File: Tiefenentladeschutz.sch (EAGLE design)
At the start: 22 parts, among them IC1 ICL7665CSA, Q4 NMOSFET-D2PAK-7, T1 BC856B

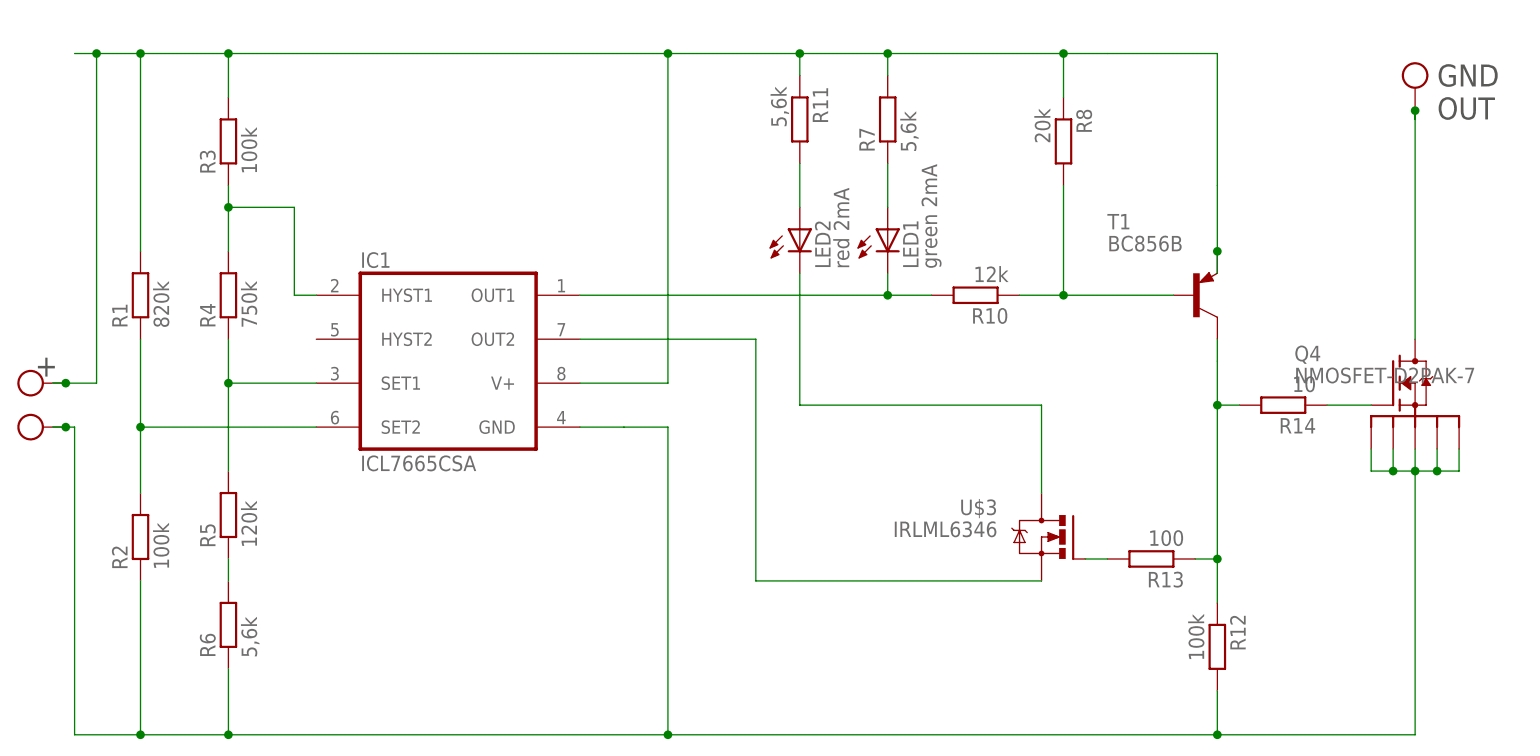
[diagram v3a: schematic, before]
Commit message: Smaller Resistors, less transistors, smaller pcb
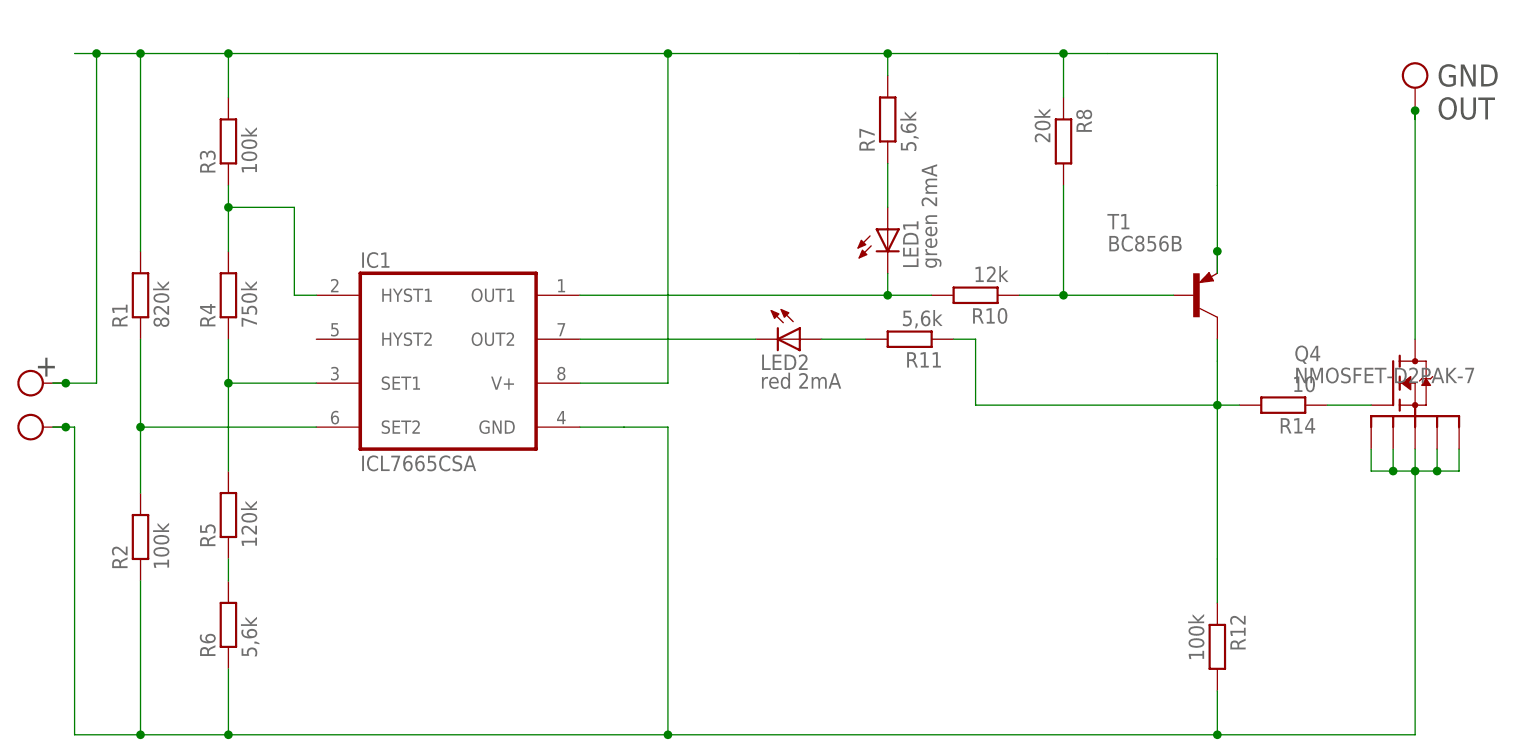
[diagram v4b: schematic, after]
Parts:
- removed R13: 100, rcl:R-EU_R1206
- removed U$3: IRLML6346, 0liver:IRLML6346
- R1, R10, R11, R2, R5, R6: device eagle-ltspice:RR1206 -> rcl:R-EU_R0603
- R3: device rcl:R-EU_R0603 -> rcl:R-EU_M1206
- U$4: device 0liver:PINBIG -> 0liver:PIN2.54
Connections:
- removed net N$11: LED2.C, U$3.D
- removed net N$9: R13.2, U$3.G
- net N$22: now also R11.1; no longer R13.1
- net N$3: now also LED2.C; no longer U$3.S
- net V+: no longer R11.1
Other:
- moved on the sheet: LED2, R11
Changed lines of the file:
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@@
 <?xml version="1.0" encoding="utf-8"?>
 <!DOCTYPE eagle SYSTEM "eagle.dtd">
-<eagle version="8.0.1">
+<eagle version="8.2.1">
 <drawing>
 <settings>
@@
 <layer number="48" name="Document" color="7" fill="1" visible="no" active="no"/>
 <layer number="49" name="Reference" color="7" fill="1" visible="no" active="no"/>
+<layer number="50" name="dxf" color="7" fill="1" visible="no" active="no"/>
 <layer number="51" name="tDocu" color="7" fill="1" visible="no" active="no"/>
 <layer number="52" name="bDocu" color="7" fill="1" visible="no" active="no"/>
+<layer number="53" name="tPadExt" color="7" fill="1" visible="no" active="no"/>
+<layer number="54" name="bPadExt" color="1" fill="1" visible="no" active="no"/>
 <layer number="90" name="Modules" color="5" fill="1" visible="yes" active="yes"/>
 <layer number="91" name="Nets" color="2" fill="1" visible="yes" active="yes"/>
@@
 <layer number="98" name="Guide" color="6" fill="1" visible="yes" active="yes"/>
 <layer number="99" name="SpiceOrder" color="5" fill="1" visible="yes" active="yes"/>
+<layer number="200" name="200bmp" color="1" fill="10" visible="no" active="no"/>
+<layer number="250" name="Descript" color="3" fill="1" visible="no" active="no"/>
+<layer number="251" name="SMDround" color="12" fill="11" visible="no" active="no"/>
 </layers>
 <schematic xreflabel="%F%N/%S.%C%R" xrefpart="/%S.%C%R">
@@
 <parts>
 <part name="R4" library="rcl" deviceset="R-EU_" device="R0603" value="750k"/>
-<part name="R5" library="eagle-ltspice" deviceset="R" device="R1206" value="120k"/>
-<part name="R1" library="eagle-ltspice" deviceset="R" device="R1206" value="820k"/>
-<part name="R2" library="eagle-ltspice" deviceset="R" device="R1206" value="100k"/>
-<part name="R11" library="eagle-ltspice" deviceset="R" device="R1206" value="5,6k"/>
+<part name="R5" library="rcl" deviceset="R-EU_" device="R0603" value="120k"/>
+<part name="R1" library="rcl" deviceset="R-EU_" device="R0603" value="820k"/>
+<part name="R2" library="rcl" deviceset="R-EU_" device="R0603" value="100k"/>
+<part name="R11" library="rcl" deviceset="R-EU_" device="R0603" value="5,6k"/>
 <part name="R8" library="rcl" deviceset="R-EU_" device="R0603" value="20k"/>
 <part name="IC1" library="maxim" deviceset="ICL7665CSA" device=""/>
@@
 <part name="LED1" library="eagle-ltspice" deviceset="LED_E" device="SML0603" value="green 2mA"/>
 <part name="R7" library="rcl" deviceset="R-EU_" device="R0603" value="5,6k"/>
-<part name="R10" library="eagle-ltspice" deviceset="R" device="R1206" value="12k"/>
-<part name="R6" library="eagle-ltspice" deviceset="R" device="R1206" value="5,6k"/>
-<part name="R3" library="rcl" deviceset="R-EU_" device="R0603" value="100k"/>
+<part name="R10" library="rcl" deviceset="R-EU_" device="R0603" value="12k"/>
+<part name="R6" library="rcl" deviceset="R-EU_" device="R0603" value="5,6k"/>
+<part name="R3" library="rcl" deviceset="R-EU_" device="M1206" value="100k"/>
 <part name="R12" library="eagle-ltspice" deviceset="R" device="R1206" value="100k"/>
-<part name="U$3" library="0liver" deviceset="IRLML6346" device=""/>
-<part name="U$4" library="0liver" deviceset="PIN" device="BIG"/>
+<part name="U$4" library="0liver" deviceset="PIN" device="2.54"/>
 <part name="U$6" library="0liver" deviceset="PIN" device="1.27"/>
 <part name="U$7" library="0liver" deviceset="PIN" device="1.27"/>
 <part name="Q4" library="D2pak-7" deviceset="NMOSFET-D2PAK-7" device=""/>
-<part name="R13" library="rcl" deviceset="R-EU_" device="R1206" value="100"/>
 <part name="R14" library="rcl" deviceset="R-EU_" device="R0603" value="10"/>
 <part name="T1" library="transistor" deviceset="*-PNP-" device="SOT23-BEC" technology="BC856B" value="BC856B"/>
@@
 <instance part="R1" gate="G$1" x="-20.32" y="68.58" rot="R90"/>
 <instance part="R2" gate="G$1" x="-20.32" y="40.64" rot="R90"/>
-<instance part="R11" gate="G$1" x="55.88" y="88.9" rot="R270"/>
+<instance part="R11" gate="G$1" x="68.58" y="63.5" rot="R180"/>
 <instance part="R8" gate="G$1" x="86.36" y="86.36" rot="R270"/>
 <instance part="IC1" gate="G$1" x="15.24" y="60.96"/>
-<instance part="LED2" gate="G$1" x="55.88" y="76.2"/>
+<instance part="LED2" gate="G$1" x="55.88" y="63.5" rot="R270"/>
 <instance part="LED1" gate="G$1" x="66.04" y="76.2"/>
 <instance part="R7" gate="G$1" x="66.04" y="88.9" rot="R90"/>
@@
 <instance part="R3" gate="G$1" x="-10.16" y="86.36" rot="R90"/>
 <instance part="R12" gate="G$1" x="104.14" y="27.94" rot="R270"/>
-<instance part="U$3" gate="G$1" x="86.36" y="40.64" rot="MR0"/>
 <instance part="U$4" gate="G$1" x="-33.02" y="58.42" rot="R90"/>
 <instance part="U$6" gate="G$1" x="-33.02" y="53.34" rot="R90"/>
 <instance part="U$7" gate="G$1" x="127" y="93.98"/>
 <instance part="Q4" gate="G$1" x="124.46" y="58.42"/>
-<instance part="R13" gate="G$1" x="96.52" y="38.1" rot="R180"/>
 <instance part="R14" gate="G$1" x="111.76" y="55.88" rot="R180"/>
 <instance part="T1" gate="G$1" x="101.6" y="68.58"/>
@@
 </segment>
 </net>
-<net name="N$5" class="0">
-<segment>
-<pinref part="R11" gate="G$1" pin="2"/>
-<pinref part="LED2" gate="G$1" pin="A"/>
-<wire x1="55.88" y1="83.82" x2="55.88" y2="78.74" width="0.1524" layer="91"/>
-</segment>
-</net>
 <net name="N$6" class="0">
 <segment>
@@
 <junction x="104.14" y="55.88"/>
 <wire x1="104.14" y1="38.1" x2="104.14" y2="55.88" width="0.1524" layer="91"/>
-<wire x1="104.14" y1="38.1" x2="101.6" y2="38.1" width="0.1524" layer="91"/>
-<junction x="104.14" y="38.1"/>
 <wire x1="104.14" y1="60.96" x2="104.14" y2="55.88" width="0.1524" layer="91"/>
 <wire x1="104.14" y1="55.88" x2="106.68" y2="55.88" width="0.1524" layer="91"/>
-<pinref part="R13" gate="G$1" pin="1"/>
 <pinref part="R14" gate="G$1" pin="2"/>
 <pinref part="T1" gate="G$1" pin="C"/>
 <wire x1="104.14" y1="63.5" x2="104.14" y2="60.96" width="0.1524" layer="91"/>
+<pinref part="R11" gate="G$1" pin="1"/>
+<wire x1="73.66" y1="63.5" x2="76.2" y2="63.5" width="0.1524" layer="91"/>
+<wire x1="76.2" y1="63.5" x2="76.2" y2="55.88" width="0.1524" layer="91"/>
+<wire x1="104.14" y1="55.88" x2="76.2" y2="55.88" width="0.1524" layer="91"/>
 </segment>
 </net>
@@
 <pinref part="R8" gate="G$1" pin="1"/>
 <wire x1="86.36" y1="96.52" x2="86.36" y2="91.44" width="0.1524" layer="91"/>
-<pinref part="R11" gate="G$1" pin="1"/>
-<wire x1="55.88" y1="96.52" x2="55.88" y2="93.98" width="0.1524" layer="91"/>
 <pinref part="R7" gate="G$1" pin="2"/>
 <wire x1="66.04" y1="96.52" x2="66.04" y2="93.98" width="0.1524" layer="91"/>
@@
 <wire x1="-20.32" y1="73.66" x2="-20.32" y2="96.52" width="0.1524" layer="91"/>
 <junction x="-20.32" y="96.52"/>
-<junction x="55.88" y="96.52"/>
 <junction x="66.04" y="96.52"/>
 <wire x1="-10.16" y1="96.52" x2="-10.16" y2="91.44" width="0.1524" layer="91"/>
@@
 </segment>
 </net>
-<net name="N$11" class="0">
-<segment>
-<pinref part="LED2" gate="G$1" pin="C"/>
-<wire x1="55.88" y1="71.12" x2="55.88" y2="55.88" width="0.1524" layer="91"/>
-<wire x1="55.88" y1="55.88" x2="83.82" y2="55.88" width="0.1524" layer="91"/>
-<wire x1="83.82" y1="55.88" x2="83.82" y2="45.72" width="0.1524" layer="91"/>
-<pinref part="U$3" gate="G$1" pin="D"/>
-</segment>
-</net>
 <net name="N$16" class="0">
 <segment>
@@
 <net name="N$3" class="0">
 <segment>
-<wire x1="83.82" y1="35.56" x2="50.8" y2="35.56" width="0.1524" layer="91"/>
-<pinref part="U$3" gate="G$1" pin="S"/>
 <pinref part="IC1" gate="G$1" pin="OUT2"/>
 <wire x1="50.8" y1="63.5" x2="30.48" y2="63.5" width="0.1524" layer="91"/>
-<wire x1="50.8" y1="35.56" x2="50.8" y2="63.5" width="0.1524" layer="91"/>
-</segment>
-</net>
-<net name="N$9" class="0">
-<segment>
-<pinref part="R13" gate="G$1" pin="2"/>
-<wire x1="91.44" y1="38.1" x2="88.9" y2="38.1" width="0.1524" layer="91"/>
-<pinref part="U$3" gate="G$1" pin="G"/>
+<pinref part="LED2" gate="G$1" pin="C"/>
 </segment>
 </net>
@@
 </segment>
 </net>
+<net name="N$5" class="0">
+<segment>
+<pinref part="LED2" gate="G$1" pin="A"/>
+<pinref part="R11" gate="G$1" pin="2"/>
+<wire x1="58.42" y1="63.5" x2="63.5" y2="63.5" width="0.1524" layer="91"/>
+</segment>
+</net>

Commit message: Some wiring adjustments
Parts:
- R1, R2: device rcl:R-EU_R0603 -> resistor:R-EU_R0603
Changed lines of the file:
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@@
 <part name="R4" library="rcl" deviceset="R-EU_" device="R0603" value="750k"/>
 <part name="R5" library="rcl" deviceset="R-EU_" device="R0603" value="120k"/>
-<part name="R1" library="rcl" deviceset="R-EU_" device="R0603" value="820k"/>
-<part name="R2" library="rcl" deviceset="R-EU_" device="R0603" value="100k"/>
+<part name="R1" library="resistor" deviceset="R-EU_" device="R0603" value="820k"/>
+<part name="R2" library="resistor" deviceset="R-EU_" device="R0603" value="100k"/>
 <part name="R11" library="rcl" deviceset="R-EU_" device="R0603" value="5,6k"/>
 <part name="R8" library="rcl" deviceset="R-EU_" device="R0603" value="20k"/>
